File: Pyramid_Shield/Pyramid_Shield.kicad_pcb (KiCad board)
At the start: 2 copper layers, 54.4 x 51.3 mm, 29 parts, among them P1 IR Rec, P2 Button, P3 RGB HEX, P4 GROVE, P5 IR LED, P6 Metal Shield, P7 CONN_5, P8 CONN_4, P9 CONN_5, Q1 PNP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

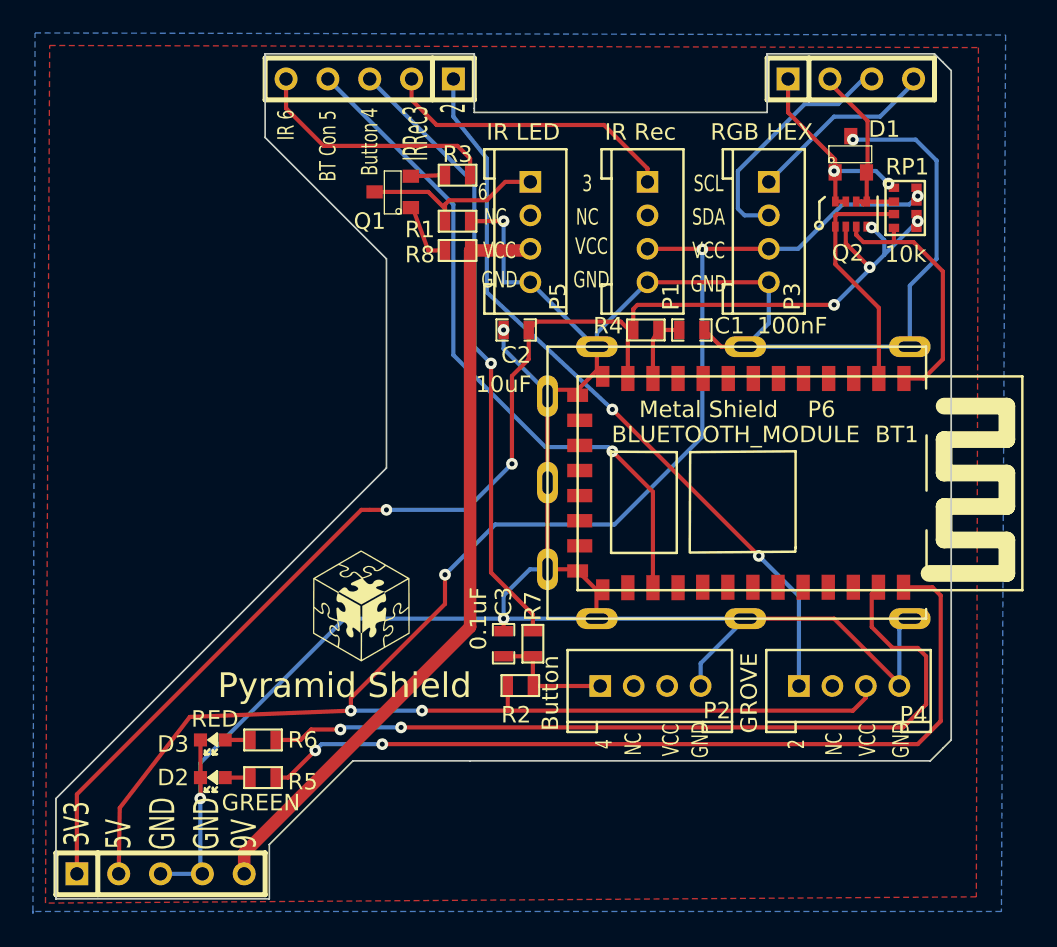
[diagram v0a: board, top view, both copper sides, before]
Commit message: fixed bugs on NPN and PNP library, IR module and Pyramid Shield
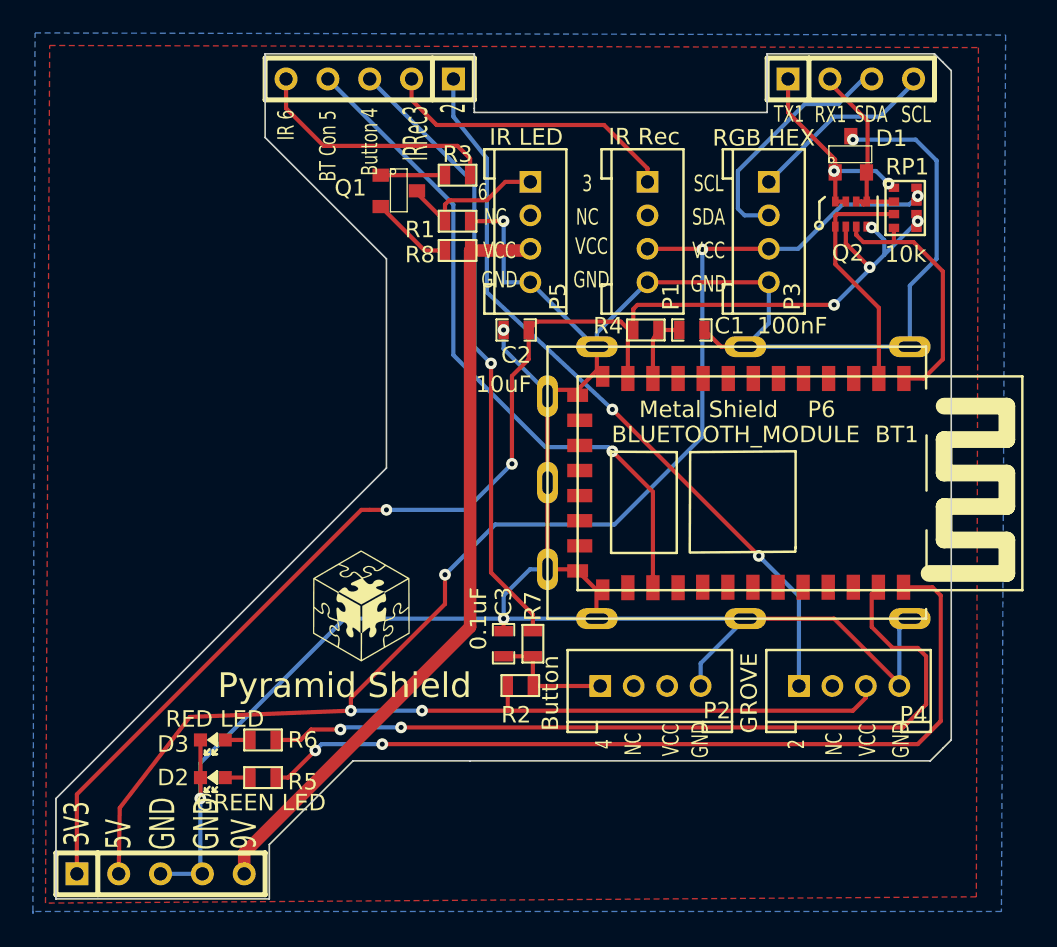
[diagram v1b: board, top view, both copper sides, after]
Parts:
- D2: value GREEN -> GREEN LED
- D3: value RED -> RED LED
- moved Q1 0.37 mm to (225.8, 120.6), turned to 270 degrees
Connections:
- R3 pad 1: N-0000038 -> N-0000039
- R8 pad 2: N-0000039 -> N-0000038
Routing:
- net N-0000038: track 2.08 -> 5.01 mm
- net N-0000040: track 12.2 -> 9.31 mm
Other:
- board text added: "RX1"
- board text added: "SCL"
- board text added: "SDA"
- board text added: "TX1"
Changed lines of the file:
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@@
     (area 190.2841 108.865999 280.796492 170.602678)
     (thickness 1.6)
-    (drawings 45)
-    (tracks 266)
+    (drawings 49)
+    (tracks 264)
     (zones 0)
     (modules 29)
@@
     (visible_elements 7FFFFFFF)
     (pcbplotparams
-      (layerselection 272400385)
+      (layerselection 284983297)
       (usegerberextensions true)
       (excludeedgelayer true)
@@
     (at 253.238 118.364)
     (tags SOT23)
-    (fp_text reference D1 (at 2.032 -1.524) (layer F.SilkS)
+    (fp_text reference D1 (at 2.4638 -0.9652) (layer F.SilkS)
       (effects (font (size 1 1) (thickness 0.15)))
     )
@@
     (pad 2 smd rect (at 0.762 0 180) (size 0.635 1.143)
       (layers F.Cu F.Paste F.Mask)
-      (net 23 N-0000039)
+      (net 22 N-0000038)
     )
     (model smd\resistors\R0603.wrl
@@
       (effects (font (size 1 1) (thickness 0.15)))
     )
-    (fp_text value RED (at -0.127 1.27 180) (layer F.SilkS)
+    (fp_text value "RED LED" (at -0.127 1.27 180) (layer F.SilkS)
       (effects (font (size 1 1) (thickness 0.15)))
     )
@@
       (effects (font (size 1 1) (thickness 0.15)))
     )
-    (fp_text value GREEN (at -2.921 -1.524 180) (layer F.SilkS)
+    (fp_text value "GREEN LED" (at -2.921 -1.524 180) (layer F.SilkS)
       (effects (font (size 1 1) (thickness 0.15)))
     )
@@
     (pad 1 smd rect (at -0.762 0) (size 0.635 1.143)
       (layers F.Cu F.Paste F.Mask)
-      (net 22 N-0000038)
+      (net 23 N-0000039)
     )
     (pad 2 smd rect (at 0.762 0) (size 0.635 1.143)
@@
   )
   (module SOT23 (layer F.Cu)
-    (at 225.425 120.65 90)
+    (at 225.7933 120.5865 270)
     (tags SOT23)
-    (fp_text reference Q1 (at -1.778 -1.397 180) (layer F.SilkS)
-      (effects (font (size 1 1) (thickness 0.15)))
-    )
-    (fp_text value PNP (at -1.524 -2.413 180) (layer F.SilkS) hide
+    (fp_text reference Q1 (at -0.1778 2.9337 360) (layer F.SilkS)
+      (effects (font (size 1 1) (thickness 0.15)))
+    )
+    (fp_text value PNP (at -1.524 -2.413 360) (layer F.SilkS) hide
       (effects (font (size 1 1) (thickness 0.15)))
     )
@@
     (fp_line (start 1.27 0.508) (end -1.3335 0.508) (layer F.SilkS) (width 0.07874))
     (fp_line (start -1.3335 -0.508) (end 1.27 -0.508) (layer F.SilkS) (width 0.07874))
-    (pad 3 smd rect (at 0 -1.09982 90) (size 0.8001 1.00076)
+    (pad 3 smd rect (at 0 -1.09982 270) (size 0.8001 1.00076)
       (layers F.Cu F.Paste F.Mask)
       (net 24 N-0000040)
     )
-    (pad 2 smd rect (at 0.9525 1.09982 90) (size 0.8001 1.00076)
+    (pad 2 smd rect (at 0.9525 1.09982 270) (size 0.8001 1.00076)
       (layers F.Cu F.Paste F.Mask)
       (net 22 N-0000038)
     )
-    (pad 1 smd rect (at -0.9525 1.09982 90) (size 0.8001 1.00076)
+    (pad 1 smd rect (at -0.9525 1.09982 270) (size 0.8001 1.00076)
       (layers F.Cu F.Paste F.Mask)
       (net 23 N-0000039)
@@
       (effects (font (size 1 1) (thickness 0.15)))
     )
-    (fp_text value "IR LED" (at 1.0922 2.3622 180) (layer F.SilkS)
+    (fp_text value "IR LED" (at 0.9144 2.0574 180) (layer F.SilkS)
       (effects (font (size 1 1) (thickness 0.15)))
     )
@@
       (effects (font (size 1 1) (thickness 0.15)))
     )
-    (fp_text value "RGB HEX" (at 1.0922 2.3622 180) (layer F.SilkS)
+    (fp_text value "RGB HEX" (at 0.9652 2.0066 180) (layer F.SilkS)
       (effects (font (size 1 1) (thickness 0.15)))
     )
@@
       (effects (font (size 1 1) (thickness 0.15)))
     )
-    (fp_text value "IR Rec" (at 1.0922 2.3622 180) (layer F.SilkS)
+    (fp_text value "IR Rec" (at 0.8636 2.0828 180) (layer F.SilkS)
       (effects (font (size 1 1) (thickness 0.15)))
     )
@@
       (net 8 /D3)
     )
+  )
+  (gr_text RX1 (at 252.0061 115.951) (layer F.SilkS)
+    (effects (font (size 1 0.7) (thickness 0.15)))
+  )
+  (gr_text TX1 (at 249.4915 115.9256) (layer F.SilkS)
+    (effects (font (size 1 0.7) (thickness 0.15)))
+  )
+  (gr_text SCL (at 257.2004 115.951) (layer F.SilkS)
+    (effects (font (size 1 0.7) (thickness 0.15)))
+  )
+  (gr_text "SDA\n" (at 254.4699 115.9383) (layer F.SilkS)
+    (effects (font (size 1 0.7) (thickness 0.15)))
   )
   (dimension 51.054632 (width 0.3) (layer Cmts.User)
@@
   (via (at 220.726 154.559) (size 0.7112) (layers F.Cu B.Cu) (net 21))
   (segment (start 219.075 156.21) (end 220.726 154.559) (width 0.254) (layer F.Cu) (net 21))
-  (segment (start 226.52482 119.6975) (end 226.6315 119.6975) (width 0.254) (layer F.Cu) (net 22) (status 30))
-  (segment (start 226.6315 119.6975) (end 228.6 119.634) (width 0.254) (layer F.Cu) (net 22) (status 10))
-  (segment (start 226.52482 121.6025) (end 226.6315 121.6025) (width 0.254) (layer F.Cu) (net 23) (status 30))
-  (segment (start 227.584 124.206) (end 228.6 124.206) (width 0.254) (layer F.Cu) (net 23))
-  (segment (start 226.6315 121.6025) (end 227.584 124.206) (width 0.254) (layer F.Cu) (net 23) (status 10))
-  (segment (start 224.32518 120.65) (end 227.584 120.65) (width 0.254) (layer F.Cu) (net 24))
-  (segment (start 228.6 121.666) (end 228.6 122.428) (width 0.254) (layer F.Cu) (net 24))
-  (segment (start 227.584 120.65) (end 228.6 121.666) (width 0.254) (layer F.Cu) (net 24))
+  (segment (start 228.6 124.206) (end 227.36048 124.206) (width 0.254) (layer F.Cu) (net 22))
+  (segment (start 227.36048 124.206) (end 224.69348 121.539) (width 0.254) (layer F.Cu) (net 22))
+  (segment (start 224.69348 119.634) (end 228.6 119.634) (width 0.254) (layer F.Cu) (net 23))
+  (segment (start 226.89312 120.5865) (end 226.89312 120.72112) (width 0.254) (layer F.Cu) (net 24))
+  (segment (start 226.89312 120.72112) (end 228.6 122.428) (width 0.254) (layer F.Cu) (net 24))
   (segment (start 228.6 122.428) (end 228.6 121.412) (width 0.254) (layer F.Cu) (net 24))
   (segment (start 232.2576 120.0404) (end 233.7816 120.0404) (width 0.254) (layer F.Cu) (net 24))
   (segment (start 231.14 121.158) (end 232.2576 120.0404) (width 0.254) (layer F.Cu) (net 24))
-  (segment (start 228.854 121.158) (end 231.14 121.158) (width 0.254) (layer F.Cu) (net 24))
+  (segment (start 228.854 121.158) (end 228.9429 121.158) (width 0.254) (layer F.Cu) (net 24))
+  (segment (start 228.9429 121.158) (end 231.14 121.158) (width 0.254) (layer F.Cu) (net 24))
   (segment (start 228.6 121.412) (end 228.854 121.158) (width 0.254) (layer F.Cu) (net 24))
   (zone (net 16) (net_name GND) (layer B.Cu) (hatch edge 0.508)

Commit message: New Product Importing
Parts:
- C3: value 0.1uF -> 100nF
- R3: value 820 -> 820R
- R5, R6, R7: value 330 -> 330R
- R8: value 200 -> 200R
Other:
- board text added: "Btn 4"
- board text added: "IR Rec3"
- board text removed: "Button 4"
- board text removed: "IRRec3"
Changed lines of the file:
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@@
     (22 B.Mask user)
     (23 F.Mask user)
-    (24 Dwgs.User user)
+    (24 Dwgs.User user hide)
     (25 Cmts.User user)
     (26 Eco1.User user)
@@
       (effects (font (size 1 1) (thickness 0.15)))
     )
-    (fp_text value 200 (at 3.81 0 180) (layer F.SilkS) hide
+    (fp_text value 200R (at 3.81 0 180) (layer F.SilkS) hide
       (effects (font (size 0.508 0.4572) (thickness 0.1143)))
     )
@@
       (effects (font (size 1 1) (thickness 0.15)))
     )
-    (fp_text value 330 (at 2.032 1.016 90) (layer F.SilkS) hide
+    (fp_text value 330R (at 2.032 1.016 90) (layer F.SilkS) hide
       (effects (font (size 0.508 0.4572) (thickness 0.1143)))
     )
@@
       (effects (font (size 1 1) (thickness 0.15)))
     )
-    (fp_text value 0.1uF (at -1.524 1.524 270) (layer F.SilkS)
+    (fp_text value 100nF (at -1.524 1.524 270) (layer F.SilkS)
       (effects (font (size 1 1) (thickness 0.15)))
     )
@@
       (effects (font (size 1 1) (thickness 0.15)))
     )
-    (fp_text value 820 (at -0.254 -2.286) (layer F.SilkS) hide
+    (fp_text value 820R (at -0.254 -2.286) (layer F.SilkS) hide
       (effects (font (size 0.508 0.4572) (thickness 0.1143)))
     )
@@
       (effects (font (size 1 1) (thickness 0.15)))
     )
-    (fp_text value 330 (at -2.413 1.016 180) (layer F.SilkS) hide
+    (fp_text value 330R (at -2.413 1.016 180) (layer F.SilkS) hide
       (effects (font (size 0.508 0.4572) (thickness 0.1143)))
     )
@@
       (effects (font (size 1 1) (thickness 0.15)))
     )
-    (fp_text value 330 (at -2.413 0.762 180) (layer F.SilkS) hide
+    (fp_text value 330R (at -2.413 0.762 180) (layer F.SilkS) hide
       (effects (font (size 0.508 0.4572) (thickness 0.1143)))
     )
@@
     (at 225.7933 120.5865 270)
     (tags SOT23)
-    (fp_text reference Q1 (at -0.1778 2.9337 360) (layer F.SilkS)
+    (fp_text reference Q1 (at 0.5715 2.8448 360) (layer F.SilkS)
       (effects (font (size 1 1) (thickness 0.15)))
     )
@@
   )
   (gr_text "Pyramid Shield" (at 222.504 150.622) (layer F.SilkS)
-    (effects (font (size 1.5 1.5) (thickness 0.3)))
+    (effects (font (size 1.5 1.5) (thickness 0.25)))
   )
   (gr_text "By Azureviolin" (at 248.666 137.16) (layer B.SilkS)
@@
   (gr_line (start 217.678 112.522) (end 217.678 117.348) (angle 90) (layer Edge.Cuts) (width 0.1))
   (gr_line (start 258.826 154.432) (end 258.064 155.194) (angle 90) (layer Edge.Cuts) (width 0.1))
-  (gr_text 2 (at 229.108 115.57 90) (layer F.SilkS)
-    (effects (font (size 1.5 0.7) (thickness 0.15)))
-  )
-  (gr_text IRRec3 (at 226.822 117.094 90) (layer F.SilkS)
-    (effects (font (size 1.5 0.7) (thickness 0.15)))
-  )
-  (gr_text "Button 4" (at 224.028 117.602 90) (layer F.SilkS)
+  (gr_text 2 (at 229.235 115.6335 90) (layer F.SilkS)
     (effects (font (size 1 0.7) (thickness 0.15)))
   )
-  (gr_text "BT Con 5" (at 221.488 117.856 90) (layer F.SilkS)
+  (gr_text "IR Rec3" (at 226.7585 117.4115 90) (layer F.SilkS)
     (effects (font (size 1 0.7) (thickness 0.15)))
   )
-  (gr_text "IR 6" (at 218.948 116.586 90) (layer F.SilkS)
+  (gr_text "Btn 4" (at 224.0915 116.7765 90) (layer F.SilkS)
     (effects (font (size 1 0.7) (thickness 0.15)))
   )
+  (gr_text "BT Con 5" (at 221.488 117.7925 90) (layer F.SilkS)
+    (effects (font (size 1 0.7) (thickness 0.15)))
+  )
+  (gr_text "IR 6" (at 218.948 116.3955 90) (layer F.SilkS)
+    (effects (font (size 1 0.7) (thickness 0.15)))
+  )
